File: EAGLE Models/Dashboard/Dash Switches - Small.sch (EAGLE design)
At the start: 14 parts

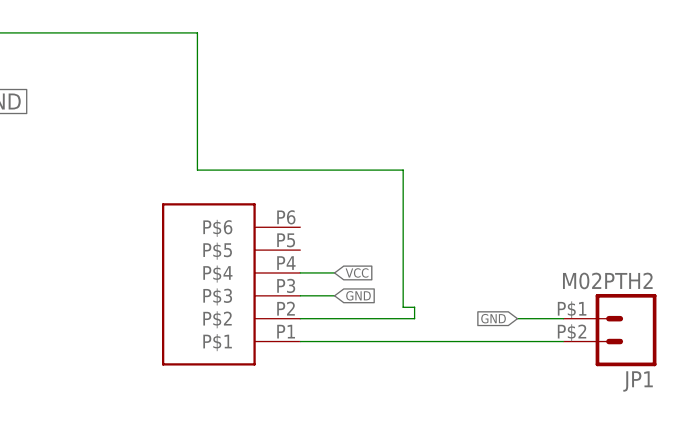
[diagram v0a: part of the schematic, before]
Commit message: Replace connectors with vias for soldering.
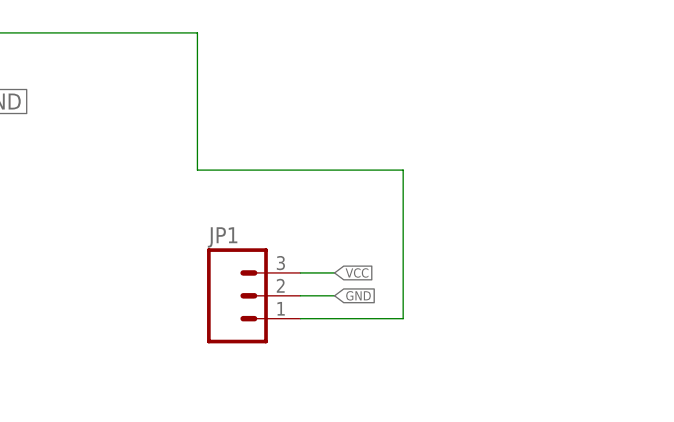
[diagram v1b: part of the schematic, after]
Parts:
- removed U$3: MICRO6LOCK, DashAndCAN library:MICRO6LOCK
- JP1: value M02PTH2 -> (none); device SparkFun-Connectors:M02PTH2 -> SparkFun-Connectors:M03PTH
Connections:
- removed net N$30: U$3.P$2
- removed net N$40: JP1.2, U$3.P$1
- net GND: now also JP1.2; no longer JP1.1, U$3.P$3
- net N$19: now also JP1.1
- net VCC: now also JP1.3; no longer U$3.P$4
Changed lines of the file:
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@@
 <part name="R20" library="rcl" deviceset="R-US_" device="R0603" value="1k"/>
 <part name="R21" library="rcl" deviceset="R-US_" device="R0603" value="1k"/>
-<part name="U$3" library="DashAndCAN library" deviceset="MICRO6LOCK" device=""/>
-<part name="JP1" library="SparkFun-Connectors" deviceset="M02" device="PTH2"/>
+<part name="JP1" library="SparkFun-Connectors" deviceset="M03" device="PTH"/>
 </parts>
 <sheets>
@@
 <instance part="R20" gate="G$1" x="-5.08" y="-64.77"/>
 <instance part="R21" gate="G$1" x="3.81" y="-72.39"/>
-<instance part="U$3" gate="G$1" x="41.91" y="-64.77" rot="R180"/>
-<instance part="JP1" gate="G$1" x="88.9" y="-67.31" rot="R180"/>
+<instance part="JP1" gate="G$1" x="44.45" y="-64.77"/>
 </instances>
 <busses>
@@
 </segment>
 <segment>
-<pinref part="U$3" gate="G$1" pin="P$4"/>
 <wire x1="52.07" y1="-62.23" x2="55.88" y2="-62.23" width="0.1524" layer="91"/>
 <label x="55.88" y="-62.23" size="1.016" layer="95" xref="yes"/>
+<pinref part="JP1" gate="G$1" pin="3"/>
 </segment>
 </net>
@@
 </segment>
 <segment>
-<pinref part="U$3" gate="G$1" pin="P$3"/>
 <wire x1="52.07" y1="-64.77" x2="55.88" y2="-64.77" width="0.1524" layer="91"/>
 <label x="55.88" y="-64.77" size="1.016" layer="95" xref="yes"/>
-</segment>
-<segment>
-<pinref part="JP1" gate="G$1" pin="1"/>
-<wire x1="81.28" y1="-67.31" x2="76.2" y2="-67.31" width="0.1524" layer="91"/>
-<label x="76.2" y="-67.31" size="1.016" layer="95" rot="R180" xref="yes"/>
-</segment>
-</net>
-<net name="N$40" class="0">
-<segment>
-<pinref part="U$3" gate="G$1" pin="P$1"/>
-<wire x1="81.28" y1="-69.85" x2="52.07" y2="-69.85" width="0.1524" layer="91"/>
 <pinref part="JP1" gate="G$1" pin="2"/>
 </segment>
@@
 <wire x1="40.64" y1="-50.8" x2="40.64" y2="-35.56" width="0.1524" layer="91"/>
 <wire x1="40.64" y1="-50.8" x2="63.5" y2="-50.8" width="0.1524" layer="91"/>
-<wire x1="63.5" y1="-50.8" x2="63.5" y2="-66.04" width="0.1524" layer="91"/>
-<wire x1="63.5" y1="-66.04" x2="64.77" y2="-66.04" width="0.1524" layer="91"/>
-<wire x1="64.77" y1="-66.04" x2="64.77" y2="-67.31" width="0.1524" layer="91"/>
+<wire x1="63.5" y1="-50.8" x2="63.5" y2="-67.31" width="0.1524" layer="91"/>
+<pinref part="JP1" gate="G$1" pin="1"/>
+<wire x1="63.5" y1="-67.31" x2="52.07" y2="-67.31" width="0.1524" layer="91"/>
 </segment>
 </net>
@@
 </segment>
 </net>
-<net name="N$30" class="0">
-<segment>
-<pinref part="U$3" gate="G$1" pin="P$2"/>
-<wire x1="64.77" y1="-67.31" x2="52.07" y2="-67.31" width="0.1524" layer="91"/>
-</segment>
-</net>
